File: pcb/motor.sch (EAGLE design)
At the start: 25 parts, among them X1 MST2V, X2 MST4V, X3 MST2V, X4 MST2V

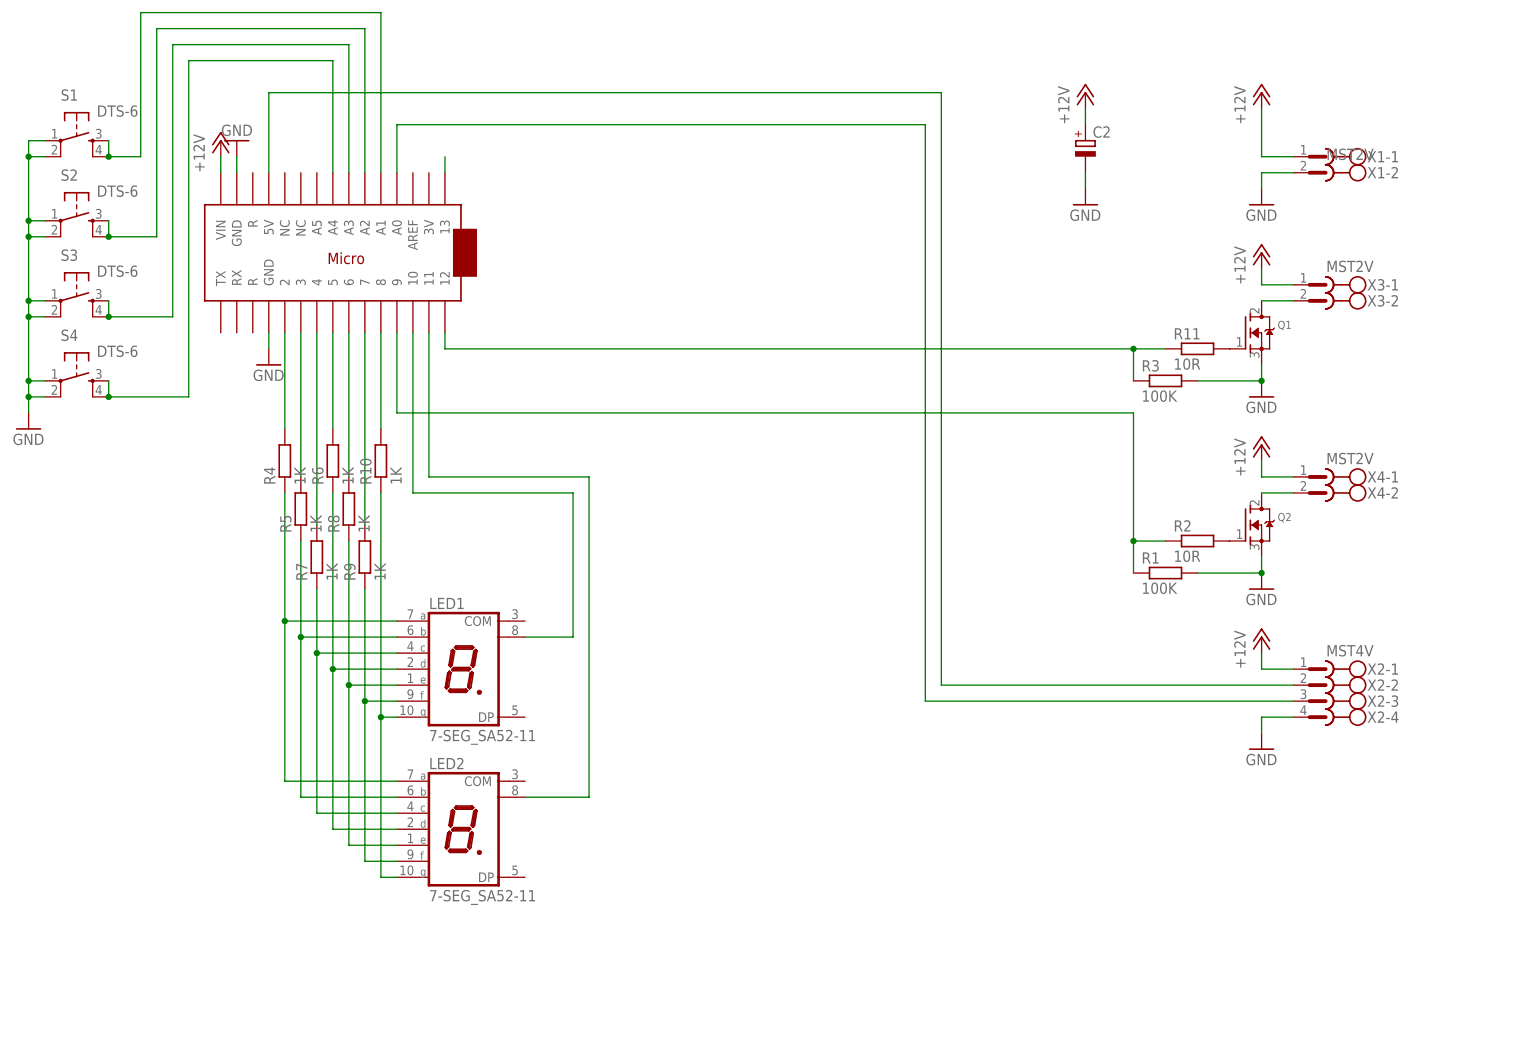
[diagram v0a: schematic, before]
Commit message: updated schematic for motor driver
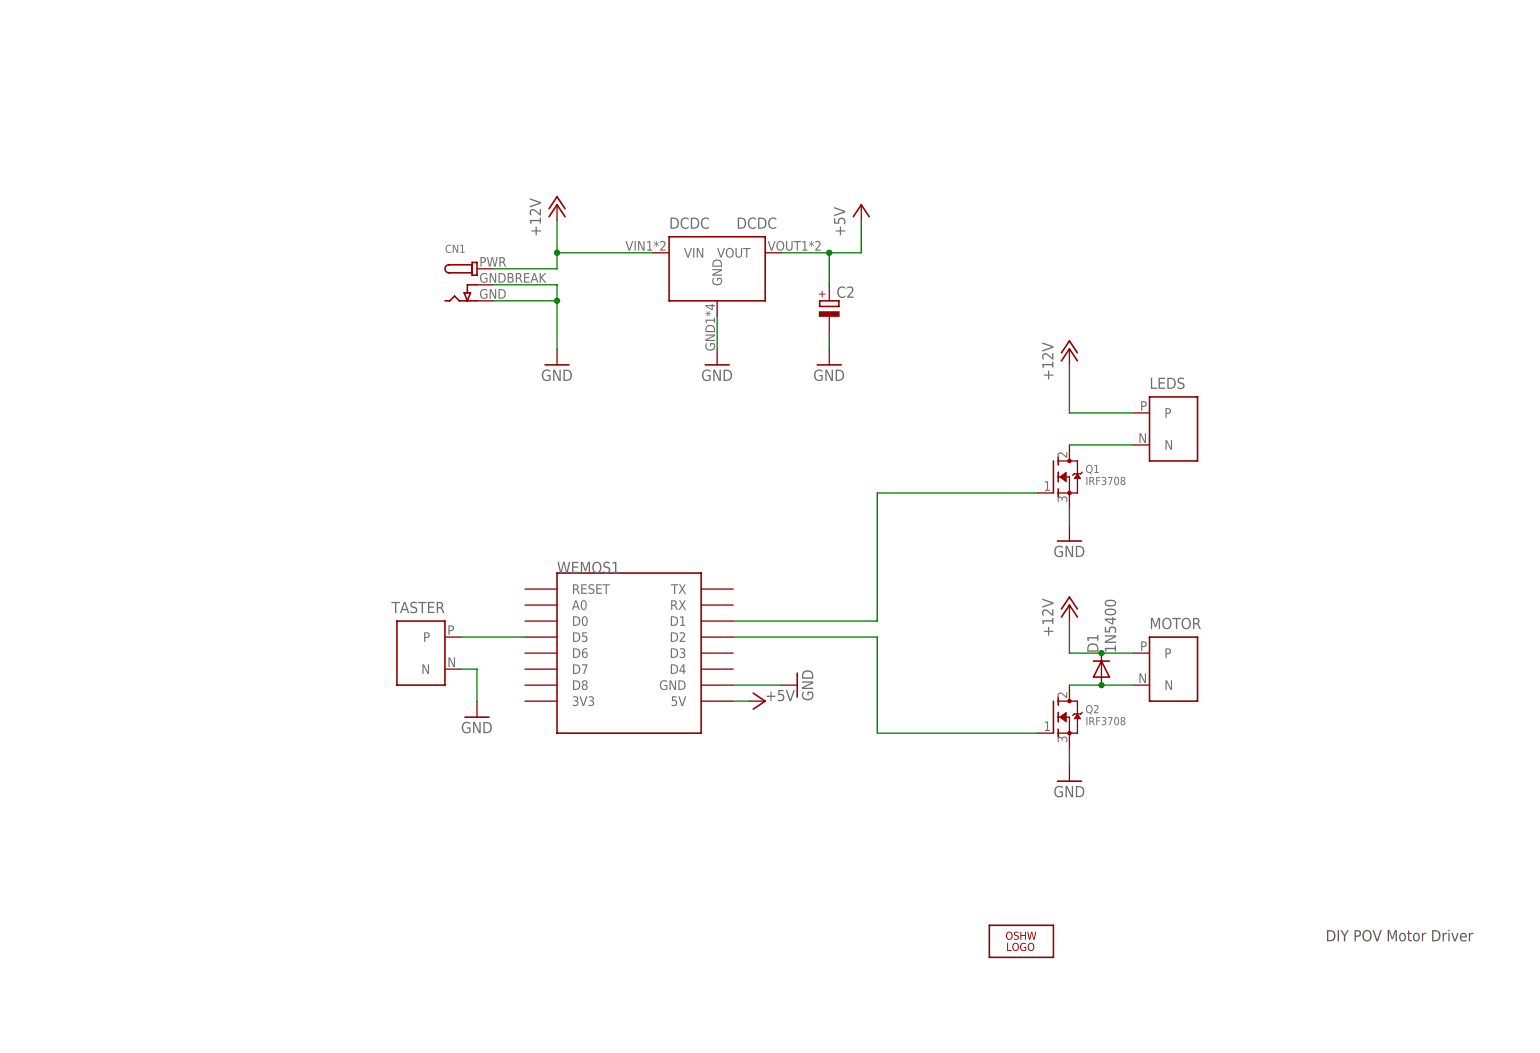
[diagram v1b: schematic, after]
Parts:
- removed LED1, LED2: 7-SEG_SA52-11, display-kingbright:7-SEG_SA52-11
- removed R1, R3: 100K, rcl:R-EU_M1206
- removed R10, R4, R5, R6, R7, R8, R9: 1K, rcl:R-EU_M1206
- removed R11, R2: 10R, rcl:R-EU_M1206
- removed S1, S2, S3, S4: DTS-6, switch-tact:DTS-6
- removed U$2: ARDUINOMICRO_NEW, adafruit:ARDUINOMICRO_NEW
- removed X1, X3, X4: MST2V, con-phoenix-508:MST2V
- removed X2: MST4V, con-phoenix-508:MST4V
- added CN1: (no value), microbuilder:DCBARRELPTH
- added D1: 1N5400, diode:1N5400
- added DCDC: DCDC, main:DCDC
- added LEDS, MOTOR, TASTER: TX30, main:TX30
- added LOGO1: OSHW_LOGO_FILLX0350-NT, ohw-logo:OSHW_LOGO_FILLX0350-NT
- added WEMOS1: (no value), esp8266modules:WEMOS-D1-MINI
- C2: device rcl:CPOL-EUE5-8.5 -> rcl:CPOL-EUE3.5-8
- Q1, Q2: value (none) -> IRF3708
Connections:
- removed net N$10: R5.2, U$2.3
- removed net N$11: LED1.F, LED2.F, R9.1
- removed net N$12: R7.2, U$2.4
- removed net N$13: R6.2, U$2.5
- removed net N$14: R8.2, U$2.6
- removed net N$15: R9.2, U$2.7
- removed net N$16: R10.2, U$2.8
- removed net N$17: U$2.13
- removed net N$18: U$2.5V, X2-2.1
- removed net N$19: S3.3, S3.4, U$2.A3
- removed net N$20: R11.1, R3.1, U$2.12
- removed net N$21: S2.3, S2.4, U$2.A2
- removed net N$22: S1.3, S1.4, U$2.A1
- removed net N$30: LED1.E, LED2.E, R8.1
- removed net N$31: LED1.D, LED2.D, R6.1
- removed net N$32: LED1.C, LED2.C, R7.1
- removed net N$33: LED1.B, LED2.B, R5.1
- removed net N$34: LED1.A, LED2.A, R4.1
- removed net N$35: LED1.COM@2, U$2.10
- removed net N$36: LED2.COM@2, U$2.11
- removed net N$6: Q2.G, R2.2
- removed net N$7: U$2.A0, X2-3.1
- removed net N$8: R4.2, U$2.2
- removed net N$9: LED1.G, LED2.G, R10.1
- new net +5V: C2.+, DCDC.VOUT, WEMOS1.5V
- net +12V: now also CN1.PWR, D1.C, DCDC.VIN, LEDS.P, MOTOR.P; no longer C2.+, U$2.VIN, X1-1.1, X2-1.1, X3-1.1, X4-1.1
- net GND: now also CN1.GND, CN1.GNDBREAK, DCDC.GND, TASTER.N, WEMOS1.GND; no longer R1.2, R3.2, S1.1, S1.2, S2.1, S2.2, S3.1, S3.2, S4.1, S4.2, U$2.GND, U$2.GND@1, X1-2.1, X2-4.1
- net N$1: now also D1.A, MOTOR.N; no longer X4-2.1
- net N$2: now also LEDS.N; no longer X3-2.1
- net N$3: now also WEMOS1.D1; no longer R11.2
- net N$4: now also TASTER.P, WEMOS1.D5; no longer S4.3, S4.4, U$2.A4
- net N$5: now also Q2.G, WEMOS1.D2; no longer R1.1, R2.1, U$2.9
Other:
- note added: "DIY POV Motor Driver"
- moved on the sheet: C2, Q1, Q2

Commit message: first version of motor driver pcb layout
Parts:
- removed DCDC: DCDC, main:DCDC
- added R1, R2: 180R, rcl:R-EU_0207/10
- added U$1: LOGO20MM, im-pro-logo:LOGO20MM
- added U$2: DCDC_5V, diypov:DCDC_5V
- C2: value (none) -> 100u
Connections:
- new net N$6: Q2.G, R2.2
- new net N$7: Q1.G, R1.2
- net +12V: now also U$2.VIN; no longer DCDC.VIN
- net +5V: now also U$2.VOUT; no longer DCDC.VOUT
- net GND: now also U$2.GND; no longer DCDC.GND
- net N$3: now also R1.1; no longer Q1.G
- net N$5: now also R2.1; no longer Q2.G
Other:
- moved on the sheet: D1, MOTOR, Q2

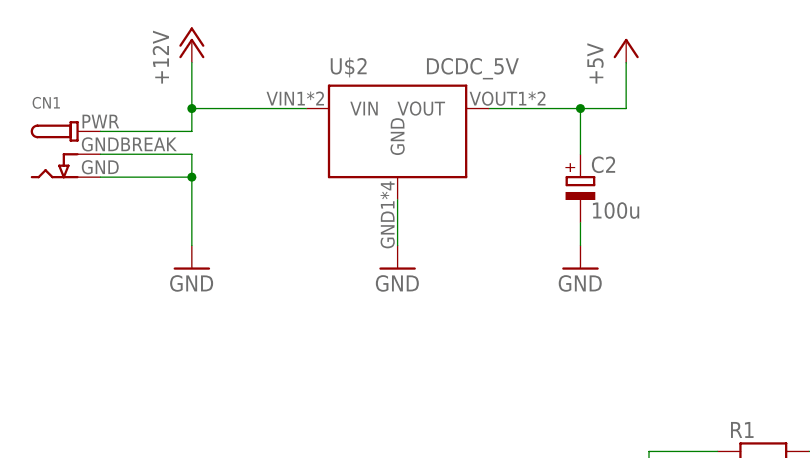
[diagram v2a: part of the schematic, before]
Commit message: finished main pcb layout
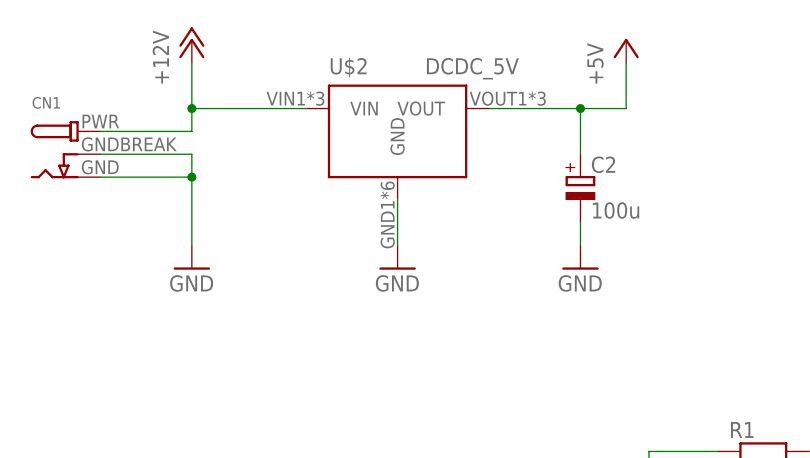
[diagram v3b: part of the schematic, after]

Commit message: layout finished
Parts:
- C2: value 100u -> 220u
- renumbered U$2 to DCDC
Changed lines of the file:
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@@
 <part name="P+4" library="supply1" deviceset="+12V" device=""/>
 <part name="P+5" library="supply1" deviceset="+5V" device=""/>
-<part name="C2" library="rcl" deviceset="CPOL-EU" device="E3.5-8" value="100u"/>
+<part name="C2" library="rcl" deviceset="CPOL-EU" device="E3.5-8" value="220u"/>
 <part name="GND7" library="supply1" deviceset="GND" device=""/>
 <part name="GND8" library="supply1" deviceset="GND" device=""/>
@@
 <part name="R2" library="rcl" deviceset="R-EU_" device="0207/10" value="180R"/>
 <part name="U$1" library="im-pro-logo" deviceset="LOGO" device="20MM" value="LOGO20MM"/>
-<part name="U$2" library="diypov" deviceset="DCDC_5V" device=""/>
+<part name="DCDC" library="diypov" deviceset="DCDC_5V" device=""/>
 </parts>
 <sheets>
@@
 <instance part="R2" gate="G$1" x="157.48" y="50.8"/>
 <instance part="U$1" gate="G$1" x="180.34" y="10.16"/>
-<instance part="U$2" gate="G$1" x="116.84" y="127"/>
+<instance part="DCDC" gate="G$1" x="116.84" y="127"/>
 </instances>
 <busses>
@@
 <pinref part="GND5" gate="1" pin="GND"/>
 <wire x1="116.84" y1="114.3" x2="116.84" y2="119.38" width="0.1524" layer="91"/>
-<pinref part="U$2" gate="G$1" pin="GND"/>
+<pinref part="DCDC" gate="G$1" pin="GND"/>
 </segment>
 <segment>
@@
 <pinref part="CN1" gate="G$1" pin="PWR"/>
 <wire x1="83.82" y1="127" x2="93.98" y2="127" width="0.1524" layer="91"/>
-<pinref part="U$2" gate="G$1" pin="VIN"/>
+<pinref part="DCDC" gate="G$1" pin="VIN"/>
 </segment>
 </net>
@@
 <junction x="137.16" y="129.54"/>
 <wire x1="127" y1="129.54" x2="137.16" y2="129.54" width="0.1524" layer="91"/>
-<pinref part="U$2" gate="G$1" pin="VOUT"/>
+<pinref part="DCDC" gate="G$1" pin="VOUT"/>
 </segment>
 <segment>
